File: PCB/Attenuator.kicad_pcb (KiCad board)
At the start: 2 copper layers, 104.2 x 26 mm, 54 parts, among them J1 In, J2 Out, J3 I2C, K1 G6K-2, K2 G6K-2, K3 G6K-2, K4 G6K-2, K5 G6K-2, K6 G6K-2, K7 G6K-2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

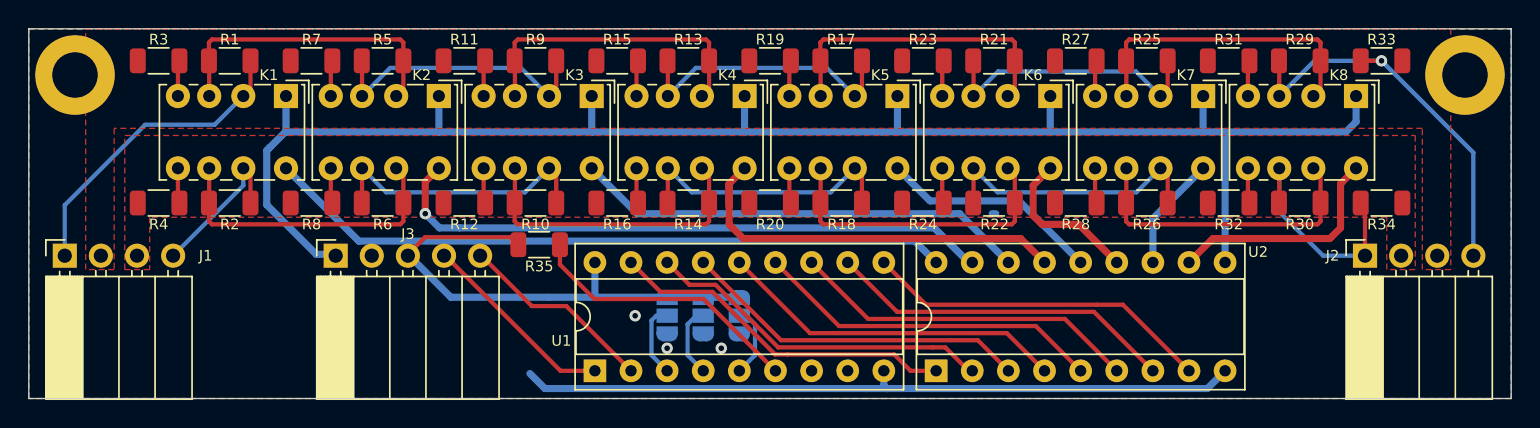
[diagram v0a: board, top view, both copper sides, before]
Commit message: Added 1u decoupling capacitors to ICs on backplane and attenuator boards
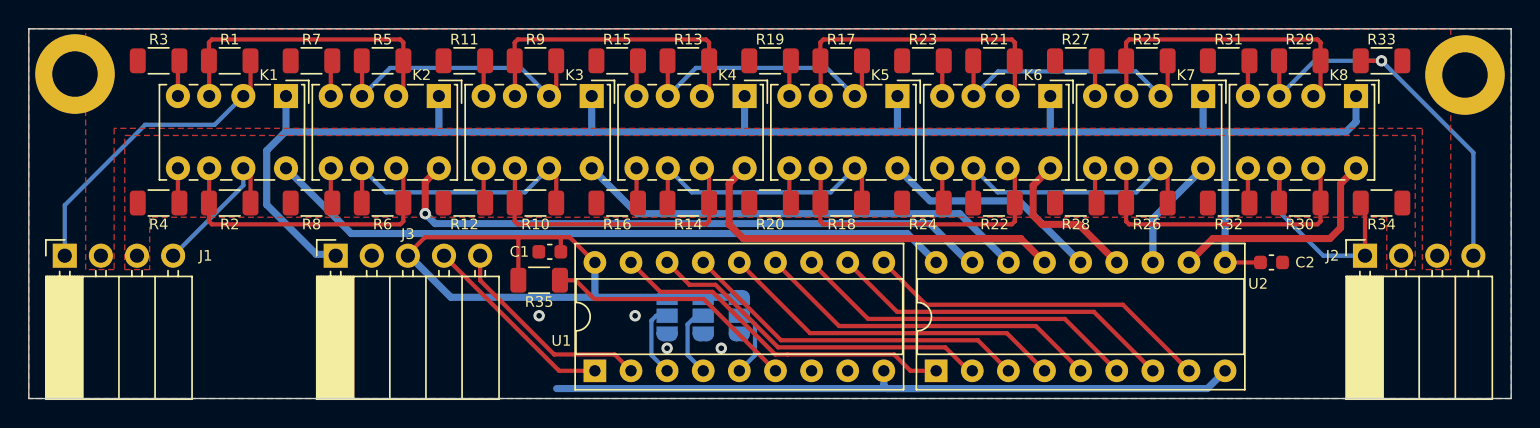
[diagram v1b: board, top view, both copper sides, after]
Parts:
- removed H3: M3, MountingHole:MountingHole_3.2mm_M3_DIN965_Pad
- added C1: 1u, Capacitor_SMD:C_0603_1608Metric, F.Cu at (48.6, 28.0)
- added C2: 1u, Capacitor_SMD:C_0603_1608Metric, F.Cu at (99.4, 28.8)
- added H2: M3, MountingHole:MountingHole_3.2mm_M3_DIN965_Pad, F.Cu at (15.2, 15.5)
- moved R35 2.50 mm to (47.9, 30.0)
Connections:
- net +12V renamed VCC
- net +3V3 renamed VDD
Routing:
- net VDD: track 35.5 -> 45.5 mm
- net VCC: track 116.6 -> 118.8 mm
- net Net-(R35-Pad2): track 19.7 -> 17.8 mm
- net Net-(K4-Pad8): track 29.3 -> 27.7 mm
- net Net-(J3-Pad5): track 14.0 -> 15.0 mm
- net GND: track 51.2 -> 51.1 mm, vias 3 -> 4

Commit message: Added bulk capacitance to each IC, rerouted 5V line on backplane board
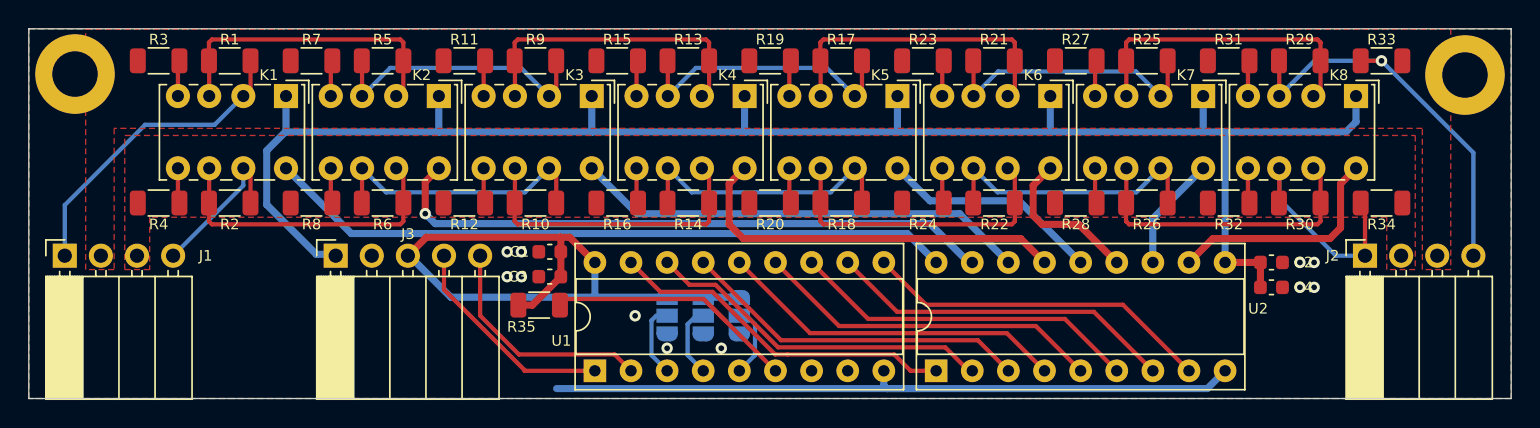
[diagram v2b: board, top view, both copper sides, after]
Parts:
- added C3: 1u, Capacitor_SMD:C_0603_1608Metric, F.Cu at (48.6, 29.8)
- added C4: 1u, Capacitor_SMD:C_0603_1608Metric, F.Cu at (99.4, 30.5)
- C1, C2: value 1u -> 100n
- moved R35 1.75 mm to (47.9, 31.8)
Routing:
- net VDD: track 45.5 -> 48.1 mm
- net VCC: track 118.8 -> 120.6 mm
- net Net-(J3-Pad5): track 15.0 -> 16.4 mm
- net Net-(J3-Pad4): track 14.0 -> 15.4 mm
- net Net-(R35-Pad2): track 17.8 -> 19.0 mm
- net Net-(J2-Pad1): track 16.1 -> 15.6 mm
- net GND: vias 4 -> 11
